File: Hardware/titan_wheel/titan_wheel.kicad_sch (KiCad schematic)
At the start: 19 parts, among them J1 REAR, J2 RPI, U1 LM358, U2 TCRT5000, U3 MLX90614

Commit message: Cleaned up schematics
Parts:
- J1: value REAR -> OTHER
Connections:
- net +5V: now also R2.2; no longer R2.1
- net at U2.A: now also R2.1; no longer R2.2
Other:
- note added: "Brake Temperature"
- note added: "Emits IR with an LED which is then reflected and picked up by a phototransistor that pulls down a line accordingly."
- note added: "Ground for reference when using test points"
- note added: "Header to provide the possibility to daisy chain the I2C lines to the other wheel if I2C is not split at the main board."
- note added: "Hysteresis Comparator"
- note added: "LED is set to light up when spoke is detected"
- note added: "Main"
- note added: "Mounting holes are mounted 21mm apart along the center of the board (10mm from bottom/top, 13.5mm in from the sides)"
- note added: "Optical Encoder"
- note added: "Other Wheel"
- note added: "Provides power from main TITAN board. Returns data from sensors over I2C (temp.) or as a 5V digital signal (encoder)."
- note added: "Thus at full reflection (presense), line is at GND"
- note added: "Two stage op-amp circuit. The threshold voltage is buffered to prevent loading effects from the hysteresis division that follows. Hysteresis is used to prevent spurrious switching near the threshold. To set the threshold, set the hysteresis potentiometer to entirely favour the threshold value (short between pins 2 and 3 on RV1) before probing TP3 and adjusting the threshold with RV2. Once that is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"
- note added: "Uses IR to measure the temperature of the brake disk. Communicates over I2C to the main TITAN board."
- note removed: "Ground for test point probing"
- moved on the sheet: C1, C2, D1, H1, H2, J1, J2, R1, R2, R3, RV1, RV2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

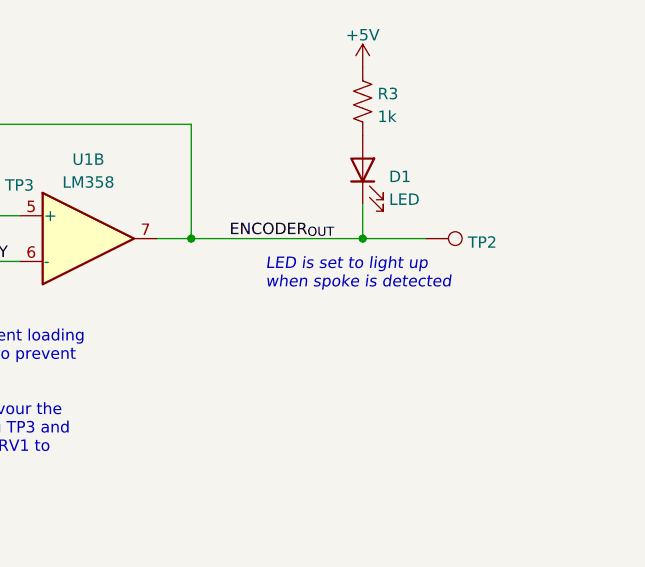
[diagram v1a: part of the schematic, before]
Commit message: Fixed note for wheel LED
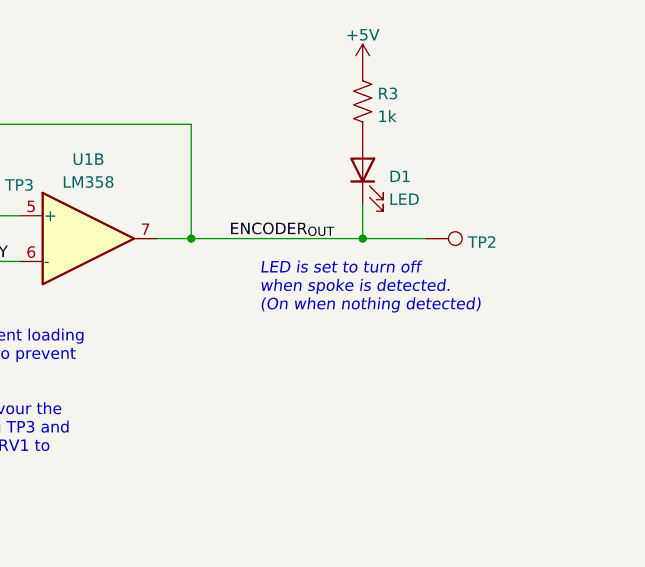
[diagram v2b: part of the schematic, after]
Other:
- note added: "LED is set to turn off when spoke is detected. (On when nothing detected)"
- note removed: "LED is set to light up when spoke is detected"
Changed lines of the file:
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@@
     (effects (font (size 2.54 2.54) (thickness 0.508) bold) (justify left bottom))
   )
-  (text "LED is set to light up \nwhen spoke is detected" (at 229.87 81.915 0)
+  (text "LED is set to turn off\nwhen spoke is detected.\n(On when nothing detected)"
+    (at 229.235 84.455 0)
     (effects (font (size 1.27 1.27) italic) (justify left bottom))
   )
